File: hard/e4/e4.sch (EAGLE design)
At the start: 16 parts

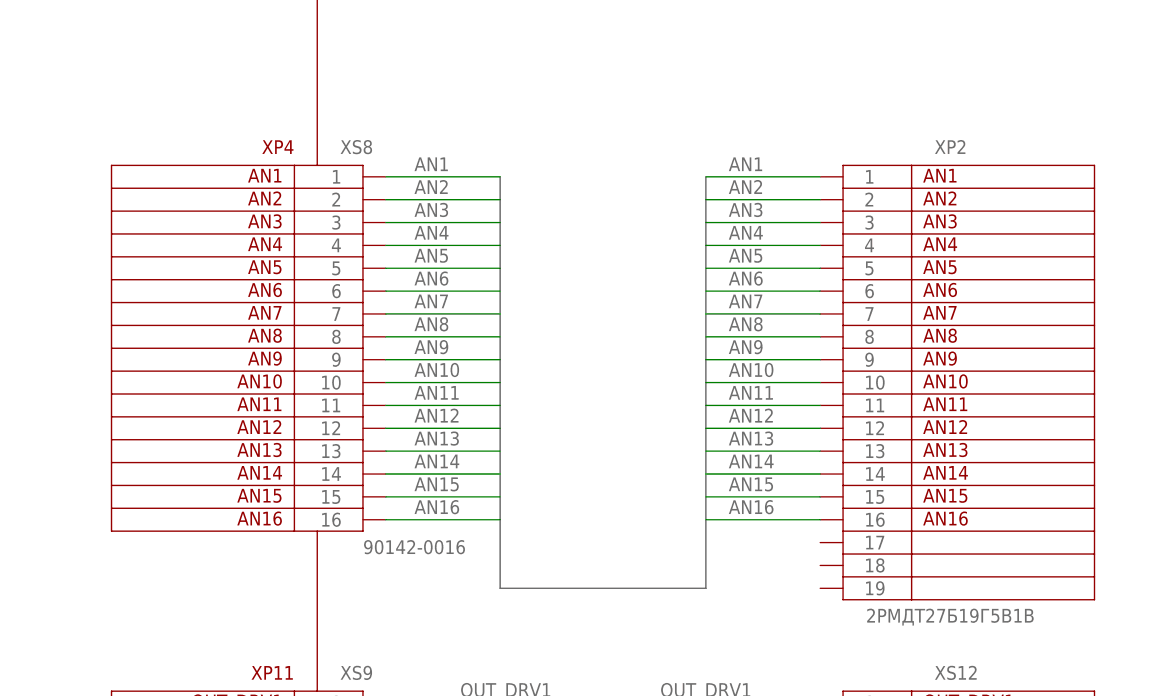
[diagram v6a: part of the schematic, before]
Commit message: nets on e4 renamed
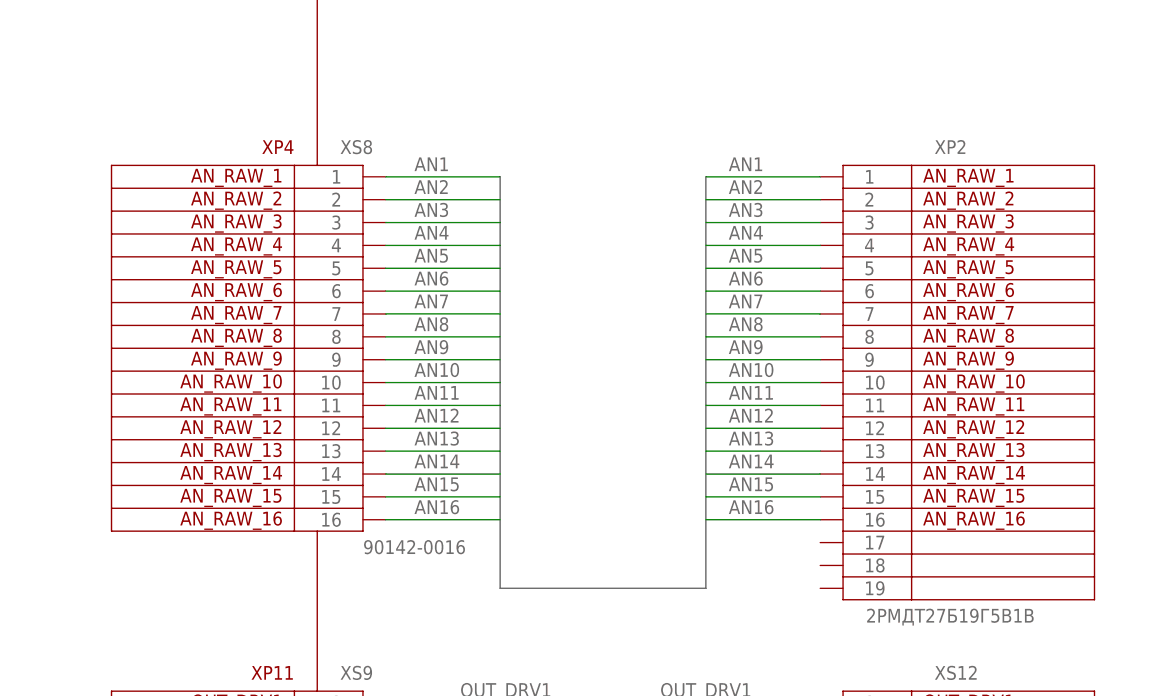
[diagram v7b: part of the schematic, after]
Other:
- note added: "AN_RAW_1"
- note added: "AN_RAW_10"
- note added: "AN_RAW_11"
- note added: "AN_RAW_12"
- note added: "AN_RAW_13"
- note added: "AN_RAW_14"
- note added: "AN_RAW_15"
- note added: "AN_RAW_16"
- note added: "AN_RAW_2"
- note added: "AN_RAW_3"
- note added: "AN_RAW_4"
- note added: "AN_RAW_5"
- note added: "AN_RAW_6"
- note added: "AN_RAW_7"
- note added: "AN_RAW_8"
- note added: "AN_RAW_9"
- note removed: "AN1"
- note removed: "AN10"
- note removed: "AN11"
- note removed: "AN12"
- note removed: "AN13"
- note removed: "AN14"
- note removed: "AN15"
- note removed: "AN16"
- note removed: "AN2"
- note removed: "AN3"
- note removed: "AN4"
- note removed: "AN5"
- note removed: "AN6"
- note removed: "AN7"
- note removed: "AN8"
- note removed: "AN9"
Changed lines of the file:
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@@
 <setting verticaltext="up"/>
 </settings>
-<grid distance="0.1" unitdist="inch" unit="inch" style="lines" multiple="1" display="yes" altdistance="0.01" altunitdist="inch" altunit="inch"/>
+<grid distance="0.1" unitdist="inch" unit="inch" style="lines" multiple="1" display="no" altdistance="0.01" altunitdist="inch" altunit="inch"/>
 <layers>
 <layer number="1" name="Top" color="4" fill="1" visible="no" active="no"/>
@@
 <sheet>
 <plain>
-<text x="257.81" y="342.265" size="1.524" layer="94">AN1</text>
-<text x="257.81" y="339.725" size="1.524" layer="94">AN2</text>
-<text x="257.81" y="337.185" size="1.524" layer="94">AN3</text>
-<text x="257.81" y="334.645" size="1.524" layer="94">AN4</text>
-<text x="257.81" y="332.105" size="1.524" layer="94">AN5</text>
-<text x="257.81" y="329.565" size="1.524" layer="94">AN6</text>
-<text x="257.81" y="327.025" size="1.524" layer="94">AN7</text>
-<text x="257.81" y="324.485" size="1.524" layer="94">AN8</text>
-<text x="257.81" y="321.945" size="1.524" layer="94">AN9</text>
-<text x="257.81" y="319.405" size="1.524" layer="94">AN10</text>
-<text x="257.81" y="316.865" size="1.524" layer="94">AN11</text>
-<text x="257.81" y="314.325" size="1.524" layer="94">AN12</text>
-<text x="257.81" y="311.785" size="1.524" layer="94">AN13</text>
-<text x="257.81" y="309.245" size="1.524" layer="94">AN14</text>
-<text x="257.81" y="306.705" size="1.524" layer="94">AN15</text>
-<text x="257.81" y="304.165" size="1.524" layer="94">AN16</text>
-<text x="186.69" y="342.265" size="1.524" layer="94" rot="MR0">AN1</text>
-<text x="186.69" y="339.725" size="1.524" layer="94" rot="MR0">AN2</text>
-<text x="186.69" y="337.185" size="1.524" layer="94" rot="MR0">AN3</text>
-<text x="186.69" y="334.645" size="1.524" layer="94" rot="MR0">AN4</text>
-<text x="186.69" y="332.105" size="1.524" layer="94" rot="MR0">AN5</text>
-<text x="186.69" y="329.565" size="1.524" layer="94" rot="MR0">AN6</text>
-<text x="186.69" y="327.025" size="1.524" layer="94" rot="MR0">AN7</text>
-<text x="186.69" y="324.485" size="1.524" layer="94" rot="MR0">AN8</text>
-<text x="186.69" y="321.945" size="1.524" layer="94" rot="MR0">AN9</text>
-<text x="186.69" y="319.405" size="1.524" layer="94" rot="MR0">AN10</text>
-<text x="186.69" y="316.865" size="1.524" layer="94" rot="MR0">AN11</text>
-<text x="186.69" y="314.325" size="1.524" layer="94" rot="MR0">AN12</text>
-<text x="186.69" y="311.785" size="1.524" layer="94" rot="MR0">AN13</text>
-<text x="186.69" y="309.245" size="1.524" layer="94" rot="MR0">AN14</text>
-<text x="186.69" y="306.705" size="1.524" layer="94" rot="MR0">AN15</text>
-<text x="186.69" y="304.165" size="1.524" layer="94" rot="MR0">AN16</text>
+<text x="186.69" y="342.265" size="1.524" layer="94" rot="MR0">AN_RAW_1</text>
+<text x="186.69" y="339.725" size="1.524" layer="94" rot="MR0">AN_RAW_2</text>
+<text x="186.69" y="337.185" size="1.524" layer="94" rot="MR0">AN_RAW_3</text>
+<text x="186.69" y="334.645" size="1.524" layer="94" rot="MR0">AN_RAW_4</text>
+<text x="186.69" y="332.105" size="1.524" layer="94" rot="MR0">AN_RAW_5</text>
+<text x="186.69" y="329.565" size="1.524" layer="94" rot="MR0">AN_RAW_6</text>
+<text x="186.69" y="327.025" size="1.524" layer="94" rot="MR0">AN_RAW_7</text>
+<text x="186.69" y="324.485" size="1.524" layer="94" rot="MR0">AN_RAW_8</text>
+<text x="186.69" y="321.945" size="1.524" layer="94" rot="MR0">AN_RAW_9</text>
+<text x="186.69" y="319.405" size="1.524" layer="94" rot="MR0">AN_RAW_10</text>
+<text x="186.69" y="316.865" size="1.524" layer="94" rot="MR0">AN_RAW_11</text>
+<text x="186.69" y="314.325" size="1.524" layer="94" rot="MR0">AN_RAW_12</text>
+<text x="186.69" y="311.785" size="1.524" layer="94" rot="MR0">AN_RAW_13</text>
+<text x="186.69" y="309.245" size="1.524" layer="94" rot="MR0">AN_RAW_14</text>
+<text x="186.69" y="306.705" size="1.524" layer="94" rot="MR0">AN_RAW_15</text>
+<text x="186.69" y="304.165" size="1.524" layer="94" rot="MR0">AN_RAW_16</text>
 <text x="17.78" y="15.24" size="3.048" layer="94">Цепи выполнить проводом МГТФ 0.35</text>
 <text x="17.78" y="10.16" size="3.048" layer="94">Для обжима использовать контакты типа 90119-2110 "Molex"</text>
@@
 <text x="46.99" y="154.305" size="1.524" layer="94" rot="MR0">REL_RAW_63</text>
 <text x="46.99" y="151.765" size="1.524" layer="94" rot="MR0">REL_RAW_64</text>
+<text x="257.81" y="342.265" size="1.524" layer="94">AN_RAW_1</text>
+<text x="257.81" y="339.725" size="1.524" layer="94">AN_RAW_2</text>
+<text x="257.81" y="337.185" size="1.524" layer="94">AN_RAW_3</text>
+<text x="257.81" y="334.645" size="1.524" layer="94">AN_RAW_4</text>
+<text x="257.81" y="332.105" size="1.524" layer="94">AN_RAW_5</text>
+<text x="257.81" y="329.565" size="1.524" layer="94">AN_RAW_6</text>
+<text x="257.81" y="327.025" size="1.524" layer="94">AN_RAW_7</text>
+<text x="257.81" y="324.485" size="1.524" layer="94">AN_RAW_8</text>
+<text x="257.81" y="321.945" size="1.524" layer="94">AN_RAW_9</text>
+<text x="257.81" y="319.405" size="1.524" layer="94">AN_RAW_10</text>
+<text x="257.81" y="316.865" size="1.524" layer="94">AN_RAW_11</text>
+<text x="257.81" y="314.325" size="1.524" layer="94">AN_RAW_12</text>
+<text x="257.81" y="311.785" size="1.524" layer="94">AN_RAW_13</text>
+<text x="257.81" y="309.245" size="1.524" layer="94">AN_RAW_14</text>
+<text x="257.81" y="306.705" size="1.524" layer="94">AN_RAW_15</text>
+<text x="257.81" y="304.165" size="1.524" layer="94">AN_RAW_16</text>
 </plain>
 <instances>

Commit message: nop
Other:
- note added: "1"
- note added: "2"
- note added: "3"
- note added: "4"
- note added: "5"
- note added: "6"
- note added: "7"
- note added: "A1"
- note added: "Crimp contacts 90119-2110 "Molex""
- note added: "KCAY.469555.025"
- note added: "Make nets from MGTF-0.35 wire"
- note added: "X1"
- note removed: "Для обжима использовать контакты типа 90119-2110 "Molex""
- note removed: "Плата КСАУ.123456.000"
- note removed: "Цепи выполнить проводом МГТФ 0.35"
